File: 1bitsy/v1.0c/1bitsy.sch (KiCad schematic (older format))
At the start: 89 parts, among them J1 BOOT, P1 CONN_01X01, P10 CONN_01X01, P11 CONN_01X01, P12 CONN_01X01, P13 CONN_01X01, P14 CONN_01X01, P15 CONN_01X01, P16 CONN_01X01, P17 CONN_01X01, P18 CONN_01X01, P19 CONN_01X01, P2 CONN_01X01, P20 CONN_01X01, P21 CONN_01X01, P22 CONN_01X01, P23 CONN_01X01, P24 USB_OTG, P25 CONN_01X01, P26 CONN_01X01, P27 CONN_01X01, P28 CONN_01X01, P29 CONN_01X01, P3 CONN_01X01, P30 CONN_01X01, P31 CONN_01X01, P32 CONN_01X01, P33 CONN_01X01, P34 CONN_01X01, P35 CONN_01X01, P36 CONN_01X01, P37 CONN_01X01, P38 CONN_01X01, P39 CONN_01X01, P4 CONN_01X01, P40 CONN_01X01, P41 CONN_01X01, P42 CONN_01X01, P43 TP, P44 TP, P45 TP, P46 TP, P47 TP, P48 CONN_01X01, P49 CONN_01X01, P5 CONN_01X01, P50 CONN_01X01, P51 CONN_01X01, P52 CONN_01X01, P53 CONN_01X01, P54 CONN_01X01, P55 CONN_01X01, P6 CONN_01X01, P7 CONN_01X01, P8 CONN_01X01, P9 CONN_01X01, SW1 TACT_G, U1 VREG_3V3, U2 STM32F415RGT, X1 32.768kHz, X2 25MHz, X3 JTAG-10

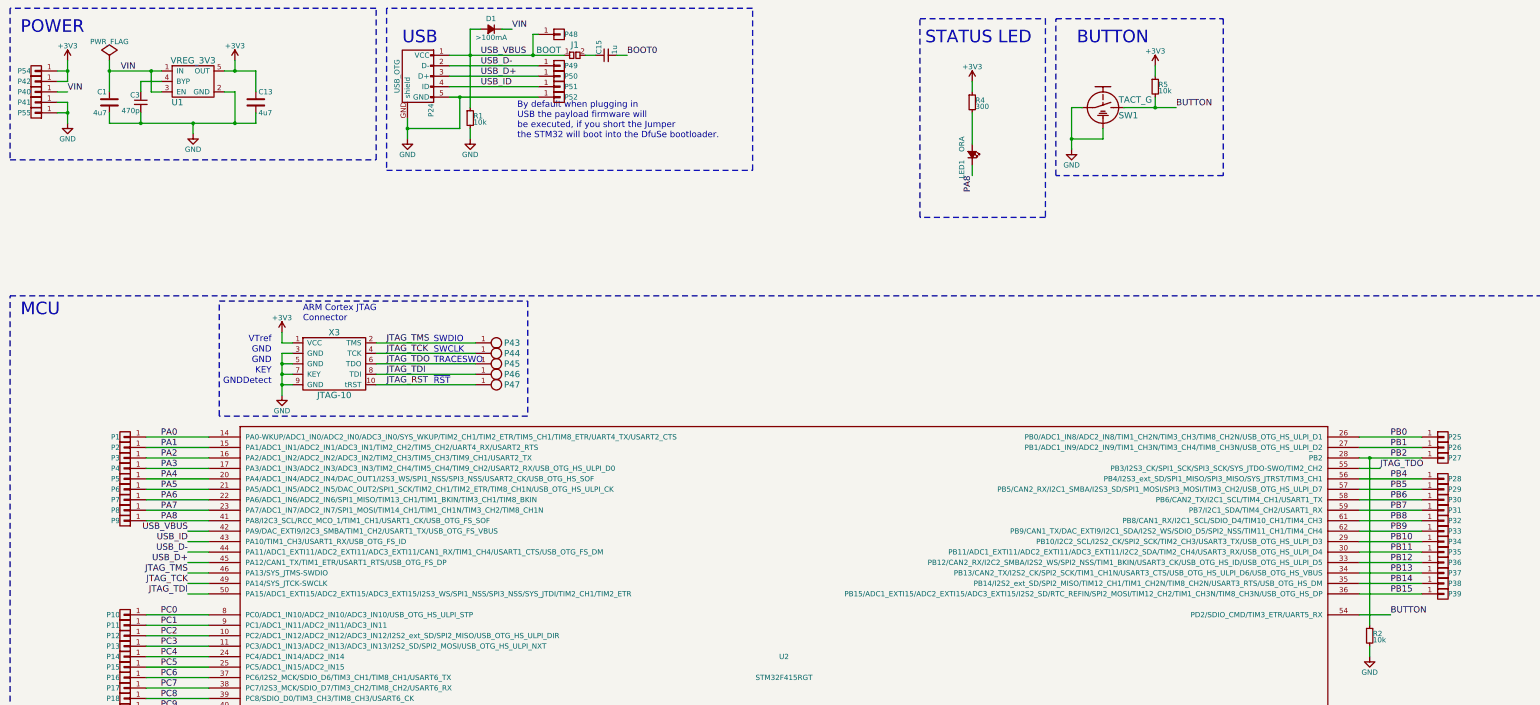
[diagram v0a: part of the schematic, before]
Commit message: Exposed the PD2 pin to allow 4pin SDIO.
The PD2 pin was connected to the button making 4bit SDIO difficult to
implement. This resulted in a bunch of IO pins changing their positions:
* Button: PD2 -> PC1
*  5: PB4 -> PD2
*  6: PB5 -> PB4
*  7: PB6 -> PB5
*  8: PB7 -> PB6
*  9: PB8 -> PB7
* 10: PB9 -> PB8
* 11: PC0 -> PB9
* XX: PC1 -> PC0
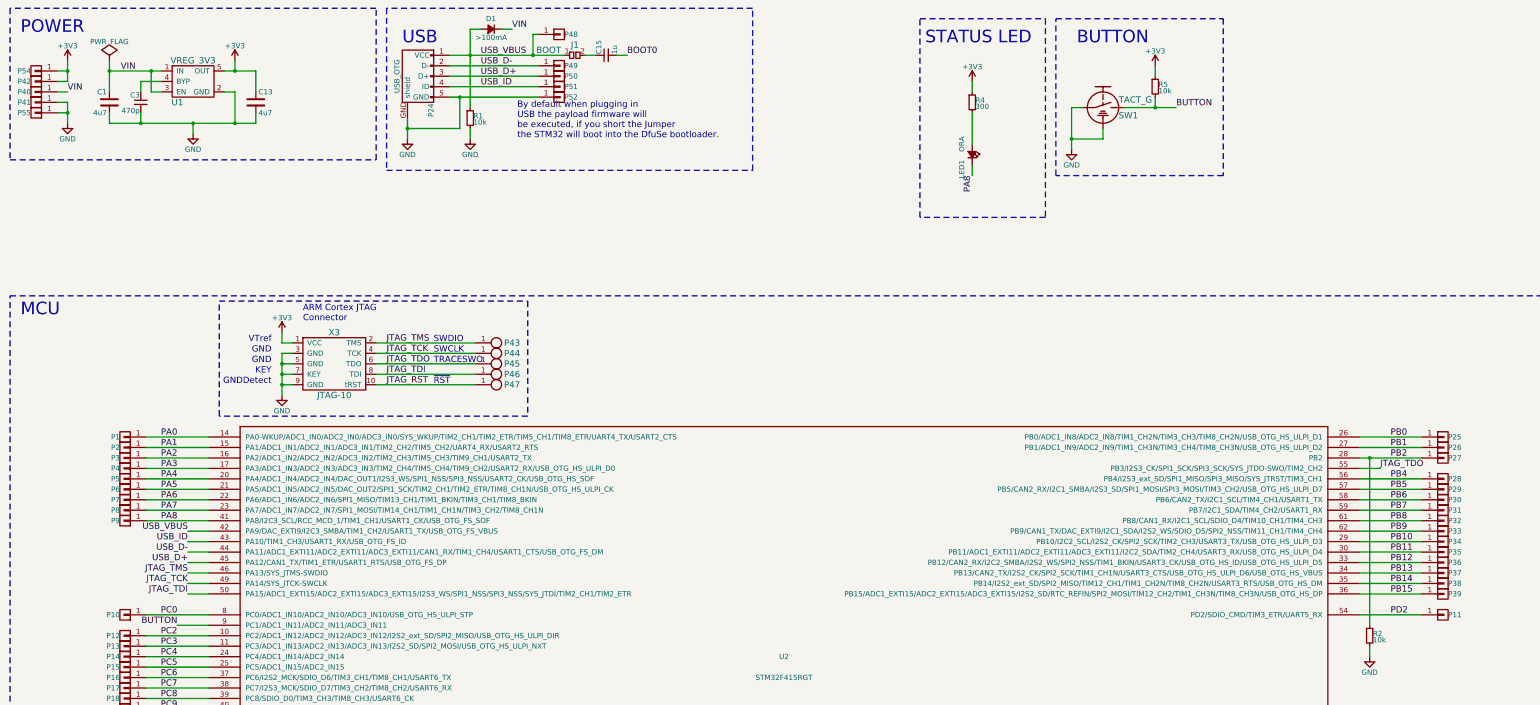
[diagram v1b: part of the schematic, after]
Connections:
- net BUTTON: now also U2.9 (PC1/ADC1_IN11/ADC2_IN11/ADC3_IN11); no longer U2.54 (PD2/SDIO_CMD/TIM3_ETR/UART5_RX)
- net PC1 renamed PD2
- net PD2: now also U2.54 (PD2/SDIO_CMD/TIM3_ETR/UART5_RX); no longer U2.9 (PC1/ADC1_IN11/ADC2_IN11/ADC3_IN11)
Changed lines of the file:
@@
 Text Label 13750 6150 0    60   ~ 0
 PB15
-Text Label 13750 6350 0    60   ~ 0
+Text Label 2150 6450 2    60   ~ 0
 BUTTON
 Text Label 2150 7650 2    60   ~ 0
@@
 Text Label 2150 6350 2    60   ~ 0
 PC0
-Text Label 2150 6450 2    60   ~ 0
-PC1
 Text Label 2150 6550 2    60   ~ 0
 PC2
@@
 	13450 6150 14050 6150
 Wire Wire Line
-	13450 6350 13750 6350
+	13450 6350 14050 6350
 Wire Wire Line
 	1850 6350 2450 6350
@@
 	2050 7650 2450 7650
 Wire Wire Line
-	1850 6450 2450 6450
+	2150 6450 2450 6450
 Wire Wire Line
 	1850 6550 2450 6550
@@
 	2600 1350 2700 1350
 Wire Wire Line
-	2700 1350 2700 1650
+	2700 1650 2700 1350
 Wire Wire Line
 	1500 1650 2900 1650
@@
 $EndComp
 $Comp
-L CONN_01X01 P11
-U 1 1 5747790E
-P 1650 6450
-F 0 "P11" H 1700 6450 50  0000 L CNN
-F 1 "CONN_01X01" V 1750 6450 50  0001 C CNN
-F 2 "pkl_pin_headers:Pin_Header_Straight_Round_1x01" H 1650 6450 50  0001 C CNN
-F 3 "" H 1650 6450 50  0000 C CNN
-F 4 "ANY" H 1650 6450 60  0001 C CNN "Source"
-	1    1650 6450
-	-1   0    0    1
-$EndComp
-$Comp
 L CONN_01X01 P12
 U 1 1 574779D7
@@
 $EndComp
 Wire Wire Line
-	1000 1250 1100 1250
-Wire Wire Line
-	1100 1250 1100 1050
+	1100 1250 1000 1250
+Wire Wire Line
+	1100 1050 1100 1250
 $Comp
 L +3V3 #PWR2
@@
 	1000 1150 1100 1150
 Connection ~ 1100 1150
+$Comp
+L CONN_01X01 P11
+U 1 1 57B9A64E
+P 14250 6350
+F 0 "P11" H 14300 6350 50  0000 L CNN
+F 1 "CONN_01X01" V 14350 6350 50  0001 C CNN
+F 2 "pkl_pin_headers:Pin_Header_Straight_Round_1x01" H 14250 6350 50  0001 C CNN
+F 3 "" H 14250 6350 50  0000 C CNN
+F 4 "ANY" H 14250 6350 60  0001 C CNN "Source"
+	1    14250 6350
+	1    0    0    -1
+$EndComp
+Text Label 13750 6350 0    60   ~ 0
+PD2
 $EndSCHEMATC

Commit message: Changed the boot jumper to 0603 size.
This should make manual soldering of it slightly easier.
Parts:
- J1: footprint pkl_jumpers:J_0402 -> pkl_jumpers:J_0603
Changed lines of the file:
@@
 F 0 "J1" H 5950 1100 60  0000 C CNN
 F 1 "BOOT" H 5700 1050 60  0000 C CNN
-F 2 "pkl_jumpers:J_0402" H 5950 1000 60  0001 C CNN
+F 2 "pkl_jumpers:J_0603" H 5950 1000 60  0001 C CNN
 F 3 "" H 5950 1000 60  0000 C CNN
 F 4 "ANY" H 5950 1000 60  0001 C CNN "Source"
